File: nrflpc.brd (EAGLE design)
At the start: 67.9 x 38.8 mm, 68 parts, among them IC1 LPC1111/12/13/14-HVQFN33, IC2 LT1763CS8-3.3, IC3 LM3401, IC5 LM3401, IC6 LM3401, IC7 LM3401, Q1 20MHz, Q2 MOSFET-PCHANNEL, Q3 MOSFET-PCHANNEL, Q4 MOSFET-PCHANNEL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

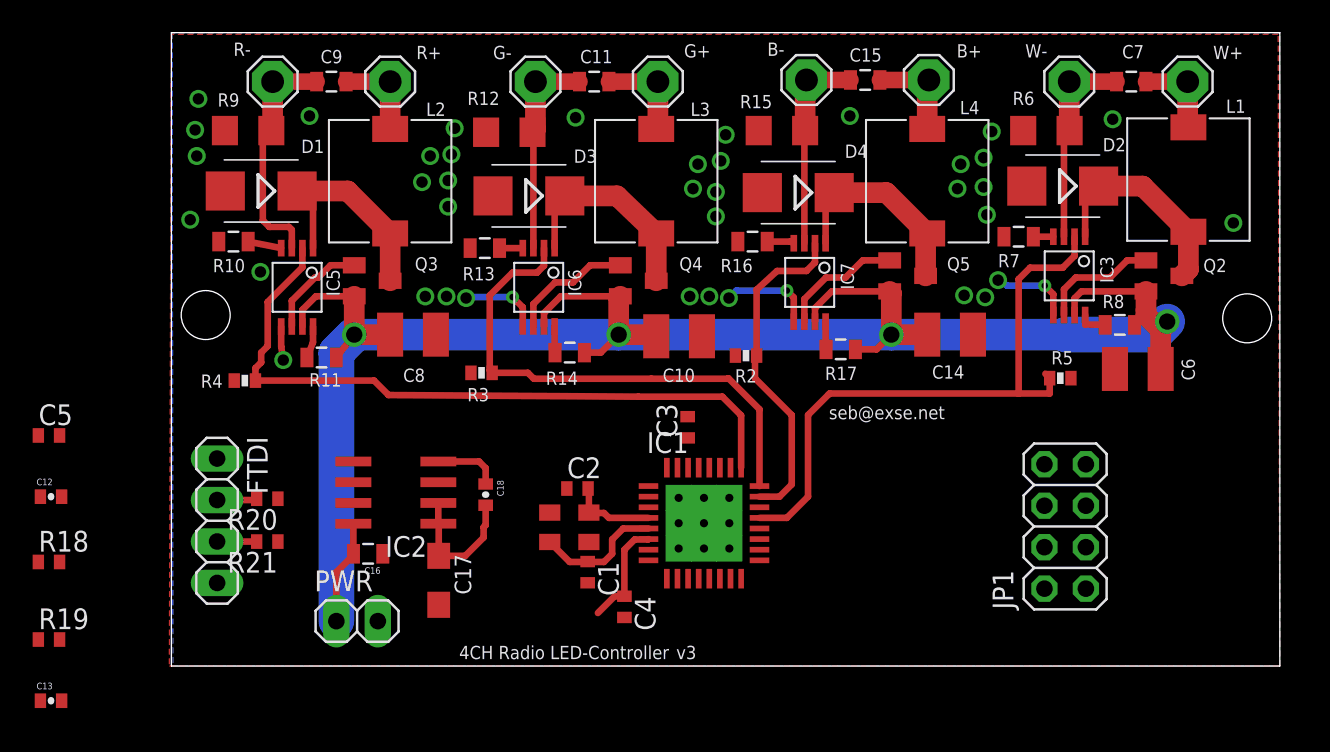
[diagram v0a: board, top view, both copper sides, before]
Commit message: Routing Voltage and "left" side (ISP)
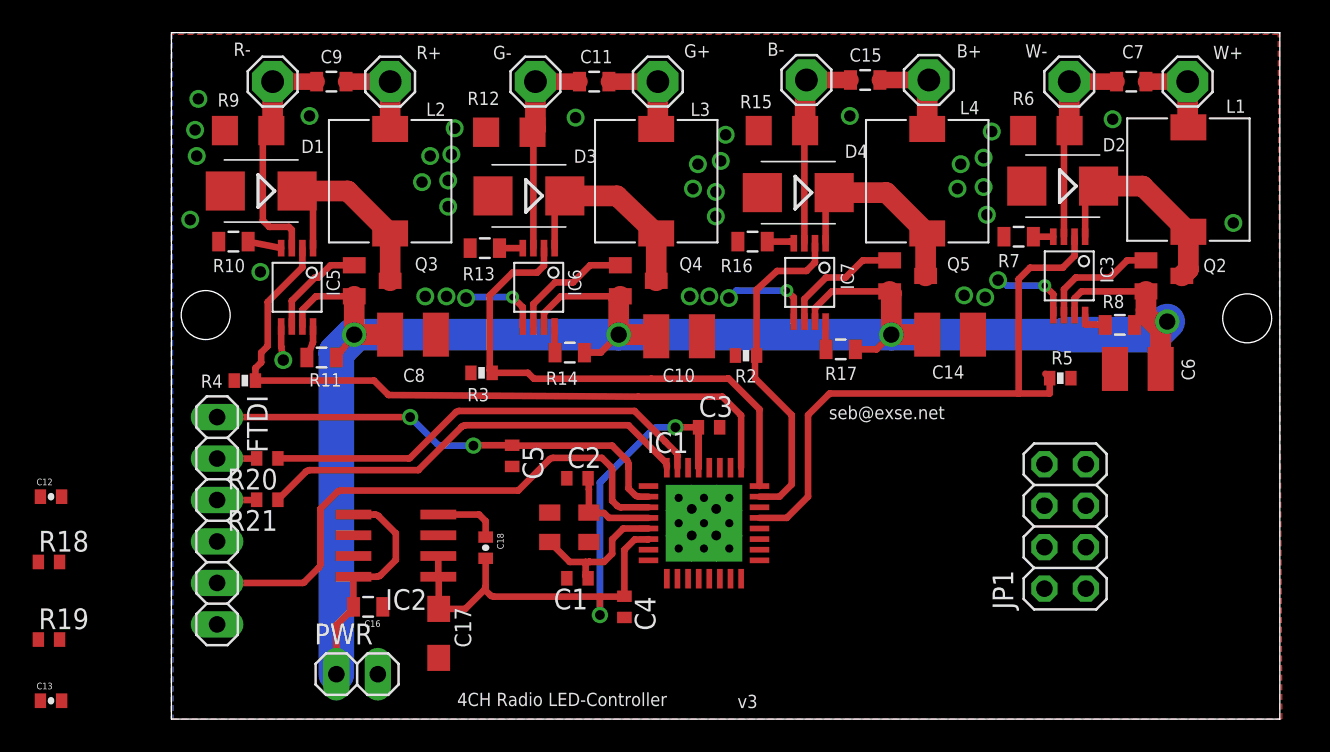
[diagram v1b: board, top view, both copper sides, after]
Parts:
- FTDI: device pinhead:1X04 -> pinhead:1X06
- moved C5 28.4 mm to (20.9, 12.9), turned to 270 degrees
- moved C16 3.25 mm to (12.1, 3.62)
- moved C17 3.25 mm to (16.4, 2.00)
- moved C18 3.25 mm to (19.2, 7.25)
- moved IC2 3.25 mm to (13.8, 7.38)
- moved PWR 3.25 mm to (11.4, -0.50)
- moved R21 2.56 mm to (5.88, 10.2)
- moved R20 2.47 mm to (5.88, 12.7)
- moved C3 1.31 mm to (32.9, 14.6), turned to 0 degrees
- moved C1 0.73 mm to (24.9, 5.38), turned to 180 degrees
- moved C2 0.62 mm to (24.9, 11.5)
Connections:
- net +12V: now also IC2.5
- net BOOTL: now also FTDI.5
- net GND: now also FTDI.6; no longer FTDI.4
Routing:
- net BOOTL: track 0.00 -> 34.0 mm
- net !RST: track 0.00 -> 29.3 mm, vias 0 -> 2
- net +3V3: track 15.1 -> 43.4 mm, vias 0 -> 2
- net N$27: track 0.00 -> 27.6 mm
- net N$30: track 0.00 -> 26.9 mm
- net +12V: track 124.4 -> 135.3 mm
- net N$29: track 8.05 -> 9.02 mm
- net N$19: track 5.28 -> 5.89 mm
- net GND: vias 41 -> 45
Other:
- board size 67.9 x 38.8 mm -> 67.9 x 42 mm

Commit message: Almost final routing
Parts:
- added EXT: (no value), pinhead:1X07
- added R1, R22: 1k, rcl:R0402
- added R23, R24, R25: 150, rcl:R0402
- moved R19 56.4 mm to (47.9, 12.4), turned to 180 degrees
- moved R18 55.9 mm to (47.9, 14.1), turned to 180 degrees
- moved C13 54.1 mm to (44.9, 11.8), turned to 90 degrees
- moved C12 52.4 mm to (44.9, 14.8), turned to 270 degrees
- moved JP1 4.83 mm to (51.9, 4.67)
- moved R20 1.00 mm to (6.88, 12.7)
- moved R21 1.00 mm to (6.88, 10.2)
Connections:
- new net N$34: IC1.9, R23.1
- new net N$35: IC1.10, R24.1
- new net N$36: IC1.11, R25.1
- net +3V3: now also EXT.6, R1.1, R22.1
- net AIN0: now also EXT.1, R1.2
- net AIN1: now also EXT.2, R22.2
- net GND: now also EXT.7
- net IO0: now also EXT.5, R23.2; no longer IC1.9
- net IO1: now also EXT.4, R24.2; no longer IC1.10
- net IO2: now also EXT.3, R25.2; no longer IC1.11
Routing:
- net +3V3: track 43.4 -> 98.4 mm, vias 2 -> 3
- net N$36: track 0.00 -> 43.4 mm
- net N$35: track 0.00 -> 43.4 mm
- net N$34: track 0.00 -> 43.3 mm
- net MISO: track 0.00 -> 26.0 mm
- net CE: track 0.00 -> 24.2 mm
- net AIN0: track 0.00 -> 22.0 mm, vias 0 -> 2
- net IRQ: track 0.00 -> 21.4 mm, vias 0 -> 1
- net AIN1: track 0.00 -> 18.0 mm
- net SCK: track 0.00 -> 17.8 mm
- net CSN: track 0.00 -> 17.1 mm
- net MOSI: track 0.00 -> 15.0 mm
- net AD1: track 0.00 -> 14.7 mm, vias 0 -> 2
- net AD6: track 0.00 -> 13.9 mm
- net IO0: track 0.00 -> 3.23 mm
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
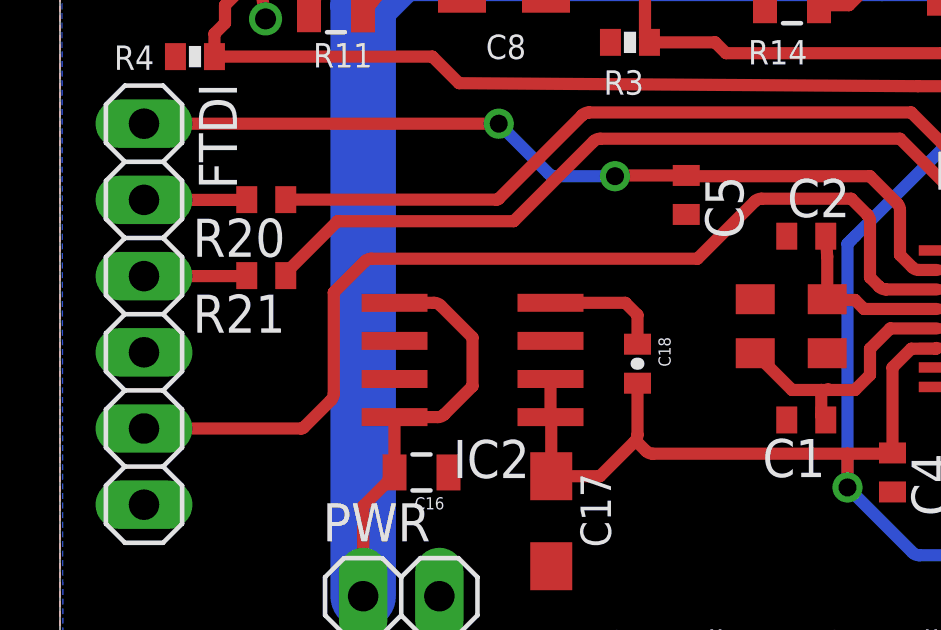
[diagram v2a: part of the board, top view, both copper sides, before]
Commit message: Fixed missing GND on IC2
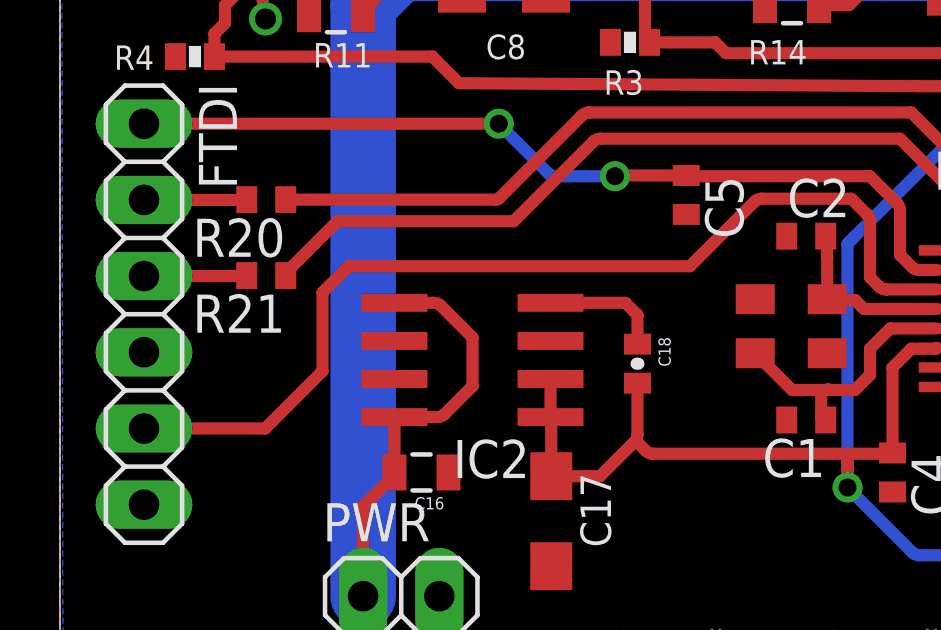
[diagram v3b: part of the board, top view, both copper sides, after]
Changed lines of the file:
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@@
 <wire x1="33.5875" y1="14.625" x2="33.375" y2="9.625" width="0" layer="19" extent="1-1"/>
 <wire x1="34.549" y1="19.0205" x2="33.5875" y2="14.625" width="0" layer="19" extent="1-1"/>
-<wire x1="11.15" y1="6.74" x2="12.95" y2="3.625" width="0" layer="19" extent="1-1"/>
+<wire x1="24.225" y1="5.375" x2="27.75" y2="2.975" width="0" layer="19" extent="1-1"/>
+<wire x1="20.875" y1="12.225" x2="24.225" y2="11.5" width="0" layer="19" extent="1-1"/>
 <wire x1="44.875" y1="11.1" x2="44.875" y2="15.4" width="0" layer="19" extent="1-1"/>
 </signal>
@@
 <wire x1="26.375" y1="12.75" x2="23.3815125" y2="12.75" width="0.4064" layer="1"/>
 <wire x1="23.3815125" y1="12.75" x2="23.15700625" y2="12.65700625" width="0.4064" layer="1" curve="45"/>
-<wire x1="23.15700625" y1="12.65700625" x2="21.25" y2="10.75" width="0.4064" layer="1"/>
-<wire x1="21.25" y1="10.75" x2="10.3815125" y2="10.75" width="0.4064" layer="1"/>
-<wire x1="10.3815125" y1="10.75" x2="10.15700625" y2="10.65700625" width="0.4064" layer="1" curve="45"/>
-<wire x1="10.15700625" y1="10.65700625" x2="9.125" y2="9.625" width="0.4064" layer="1"/>
-<wire x1="9.125" y1="9.625" x2="9.125" y2="6.2565125" width="0.4064" layer="1"/>
-<wire x1="9.125" y1="6.2565125" x2="9.03200625" y2="6.03200625" width="0.4064" layer="1" curve="-45"/>
-<wire x1="9.03200625" y1="6.03200625" x2="8.125" y2="5.125" width="0.4064" layer="1"/>
-<wire x1="2.8" y1="5.09" x2="8.040503125" y2="5.09" width="0.4064" layer="1"/>
-<wire x1="8.040503125" y1="5.09" x2="8.125" y2="5.125" width="0.4064" layer="1" curve="45"/>
+<wire x1="23.15700625" y1="12.65700625" x2="21" y2="10.5" width="0.4064" layer="1"/>
+<wire x1="21" y1="10.5" x2="9.625" y2="10.5" width="0.4064" layer="1"/>
+<wire x1="9.625" y1="10.5" x2="8.75" y2="9.625" width="0.4064" layer="1"/>
+<wire x1="8.75" y1="9.625" x2="8.75" y2="7" width="0.4064" layer="1"/>
+<wire x1="8.75" y1="7" x2="6.84" y2="5.09" width="0.4064" layer="1"/>
+<wire x1="6.84" y1="5.09" x2="2.8" y2="5.09" width="0.4064" layer="1"/>
 </signal>
 <signal name="N$18">

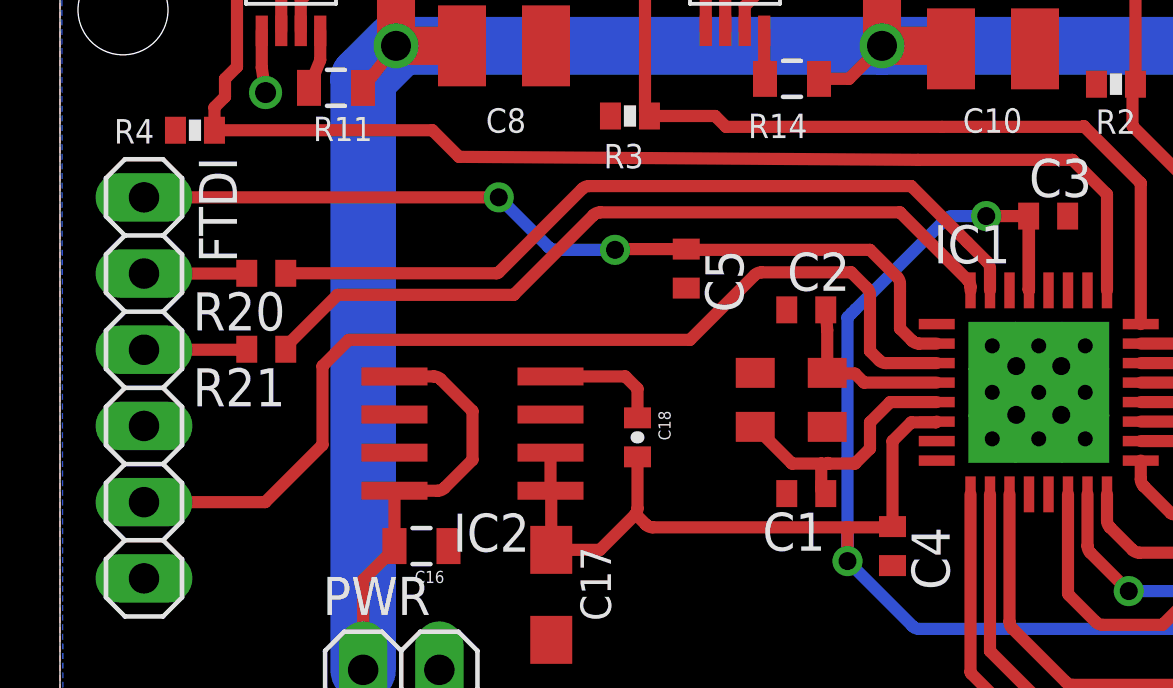
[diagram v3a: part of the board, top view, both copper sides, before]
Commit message: Fixed even more GND problems
MORE GND!!!
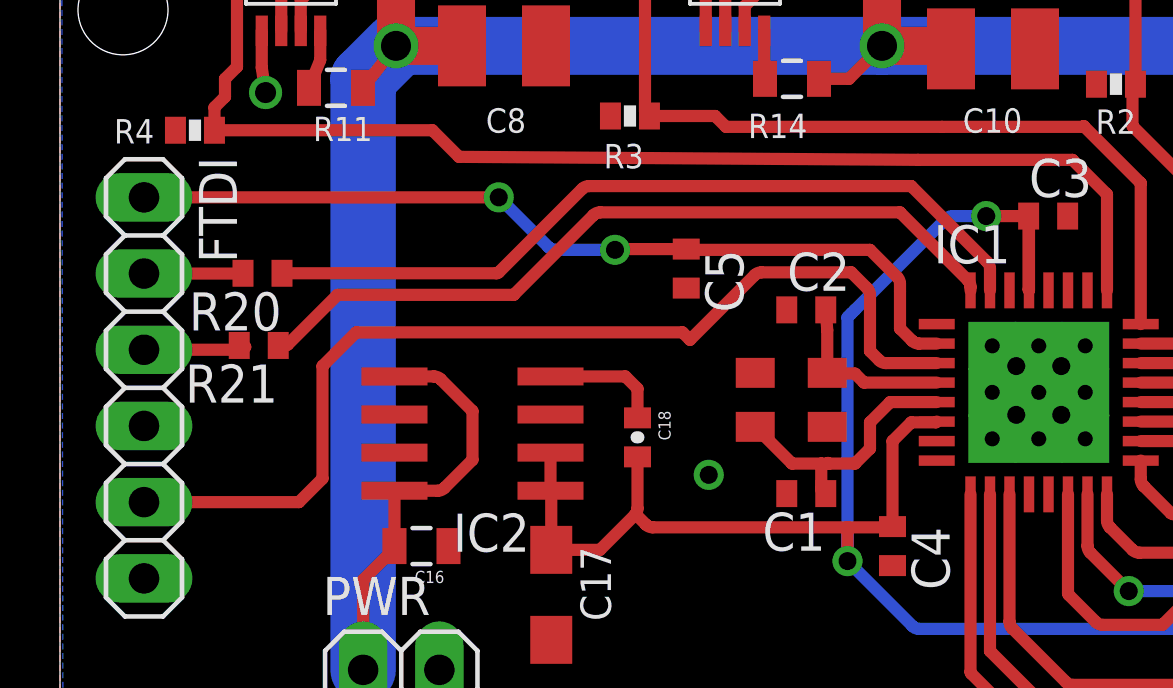
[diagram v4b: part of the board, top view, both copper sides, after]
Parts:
- moved R21 0.28 mm to (6.62, 10.3)
- moved R20 0.12 mm to (6.75, 12.7)
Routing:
- net BOOTL: track 33.5 -> 34.4 mm
- net GND: vias 45 -> 46
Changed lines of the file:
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@@
 <element name="C13" library="SparkFun" package="0402-CAP" value="200pF" x="44.875" y="11.75" rot="R90"/>
 <element name="R19" library="rcl" package="R0402" value="4.7k" x="47.875" y="12.375" rot="R180"/>
-<element name="R20" library="rcl" package="R0402" value="150" x="6.875" y="12.71875" rot="R180"/>
-<element name="R21" library="rcl" package="R0402" value="150" x="6.875" y="10.1875" rot="R180"/>
+<element name="R20" library="rcl" package="R0402" value="150" x="6.75" y="12.71875" rot="R180"/>
+<element name="R21" library="rcl" package="R0402" value="150" x="6.625" y="10.3125" rot="R180"/>
 <element name="IC2" library="linear-technology" package="SOIC8" value="LT1763CS8-3.3" x="13.75" y="7.375" rot="R90">
 <attribute name="OC_NEWARK" value="57M6055" x="13.75" y="7.375" size="1.778" layer="27" rot="R90" display="off"/>
@@
 <contactref element="FTDI" pad="2"/>
 <wire x1="2.8" y1="12.71" x2="6.203875" y2="12.71" width="0.4064" layer="1"/>
-<wire x1="6.203875" y1="12.71" x2="6.225" y2="12.71875" width="0.4064" layer="1" curve="45"/>
+<wire x1="6.203875" y1="12.71" x2="6.1" y2="12.71875" width="0.4064" layer="1" curve="45"/>
 </signal>
 <signal name="PB">
@@
 <wire x1="2.8" y1="10.17" x2="5.9509875" y2="10.17" width="0.4064" layer="1"/>
 <wire x1="5.9509875" y1="10.17" x2="6.17549375" y2="10.26299375" width="0.4064" layer="1" curve="45"/>
-<wire x1="6.17549375" y1="10.26299375" x2="6.225" y2="10.1875" width="0.4064" layer="1"/>
+<wire x1="6.17549375" y1="10.26299375" x2="5.975" y2="10.3125" width="0.4064" layer="1"/>
 </signal>
 <signal name="GND">
@@
 <via x="31.875" y="8" extent="1-16" drill="0.6" diameter="0.4064"/>
 <contactref element="EXT" pad="7"/>
+<via x="21.625" y="6" extent="1-16" drill="0.6"/>
 <wire x1="32.625" y1="8.75" x2="33.375" y2="9.625" width="0" layer="19" extent="1-1"/>
 <wire x1="33.375" y1="8" x2="32.625" y2="8.75" width="0" layer="19" extent="1-1"/>
@@
 <wire x1="33.5875" y1="14.625" x2="33.375" y2="9.625" width="0" layer="19" extent="1-1"/>
 <wire x1="34.549" y1="19.0205" x2="33.5875" y2="14.625" width="0" layer="19" extent="1-1"/>
-<wire x1="24.225" y1="5.375" x2="27.75" y2="2.975" width="0" layer="19" extent="1-1"/>
-<wire x1="20.875" y1="12.225" x2="24.225" y2="11.5" width="0" layer="19" extent="1-1"/>
 <wire x1="44.875" y1="11.1" x2="44.875" y2="15.4" width="0" layer="19" extent="1-1"/>
 </signal>
@@
 <wire x1="31" y1="12.15" x2="31" y2="12.8684875" width="0.4064" layer="1"/>
 <wire x1="31" y1="12.8684875" x2="30.90700625" y2="13.09299375" width="0.4064" layer="1" curve="45"/>
-<wire x1="30.90700625" y1="13.09299375" x2="30.25" y2="13.75" width="0.4064" layer="1"/>
-<wire x1="30.25" y1="13.75" x2="28.375" y2="15.625" width="0.4064" layer="1"/>
+<wire x1="30.90700625" y1="13.09299375" x2="28.375" y2="15.625" width="0.4064" layer="1"/>
 <wire x1="28.375" y1="15.625" x2="17.6315125" y2="15.625" width="0.4064" layer="1"/>
 <wire x1="17.6315125" y1="15.625" x2="17.40700625" y2="15.53200625" width="0.4064" layer="1" curve="45"/>
 <wire x1="17.40700625" y1="15.53200625" x2="14.625" y2="12.75" width="0.4064" layer="1"/>
 <wire x1="14.54955625" y1="12.71875" x2="14.625" y2="12.75" width="0.4064" layer="1" curve="45"/>
-<wire x1="7.525" y1="12.71875" x2="14.54955625" y2="12.71875" width="0.4064" layer="1"/>
+<wire x1="7.4" y1="12.71875" x2="14.54955625" y2="12.71875" width="0.4064" layer="1"/>
 </signal>
 <signal name="N$30">
@@
 <wire x1="18.0065125" y1="14.75" x2="17.78200625" y2="14.65700625" width="0.4064" layer="1" curve="45"/>
 <wire x1="17.78200625" y1="14.65700625" x2="15.125" y2="12" width="0.4064" layer="1"/>
-<wire x1="7.525" y1="10.1875" x2="7.586871875" y2="10.336871875" width="0.4064" layer="1" curve="-45"/>
+<wire x1="7.275" y1="10.3125" x2="7.586871875" y2="10.336871875" width="0.4064" layer="1" curve="-45"/>
 <wire x1="7.586871875" y1="10.336871875" x2="9.25" y2="12" width="0.4064" layer="1"/>
 <wire x1="9.25" y1="12" x2="15.125" y2="12" width="0.4064" layer="1"/>
@@
 <wire x1="23.3815125" y1="12.75" x2="23.15700625" y2="12.65700625" width="0.4064" layer="1" curve="45"/>
 <wire x1="23.15700625" y1="12.65700625" x2="21" y2="10.5" width="0.4064" layer="1"/>
-<wire x1="21" y1="10.5" x2="9.625" y2="10.5" width="0.4064" layer="1"/>
-<wire x1="9.625" y1="10.5" x2="8.75" y2="9.625" width="0.4064" layer="1"/>
-<wire x1="8.75" y1="9.625" x2="8.75" y2="7" width="0.4064" layer="1"/>
-<wire x1="8.75" y1="7" x2="6.84" y2="5.09" width="0.4064" layer="1"/>
-<wire x1="6.84" y1="5.09" x2="2.8" y2="5.09" width="0.4064" layer="1"/>
+<wire x1="21" y1="10.5" x2="20.75" y2="10.75" width="0.4064" layer="1"/>
+<wire x1="20.75" y1="10.75" x2="9.875" y2="10.75" width="0.4064" layer="1"/>
+<wire x1="9.875" y1="10.75" x2="8.75" y2="9.625" width="0.4064" layer="1"/>
+<wire x1="8.75" y1="9.625" x2="8.75" y2="5.875" width="0.4064" layer="1"/>
+<wire x1="8.75" y1="5.875" x2="7.965" y2="5.09" width="0.4064" layer="1"/>
+<wire x1="7.965" y1="5.09" x2="2.8" y2="5.09" width="0.4064" layer="1"/>
 </signal>
 <signal name="N$18">
